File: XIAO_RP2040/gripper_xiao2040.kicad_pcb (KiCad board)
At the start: 2 copper layers, 11 parts, among them J1 GoFa IO, J2 VGoFa, J3 Servo, U1 XIAO-RP2040-DIP, U2 HCPL-2631

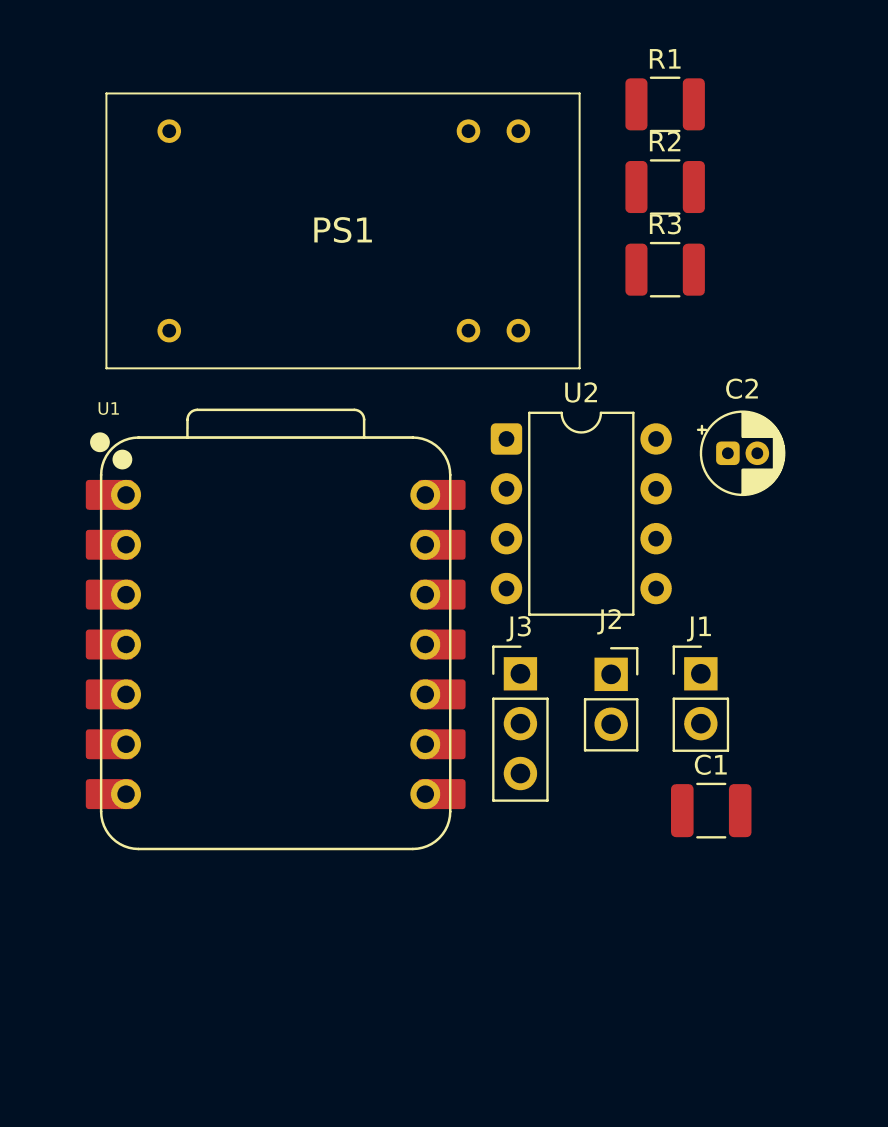
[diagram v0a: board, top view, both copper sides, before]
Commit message: Improving PCB routing and including Arduino code
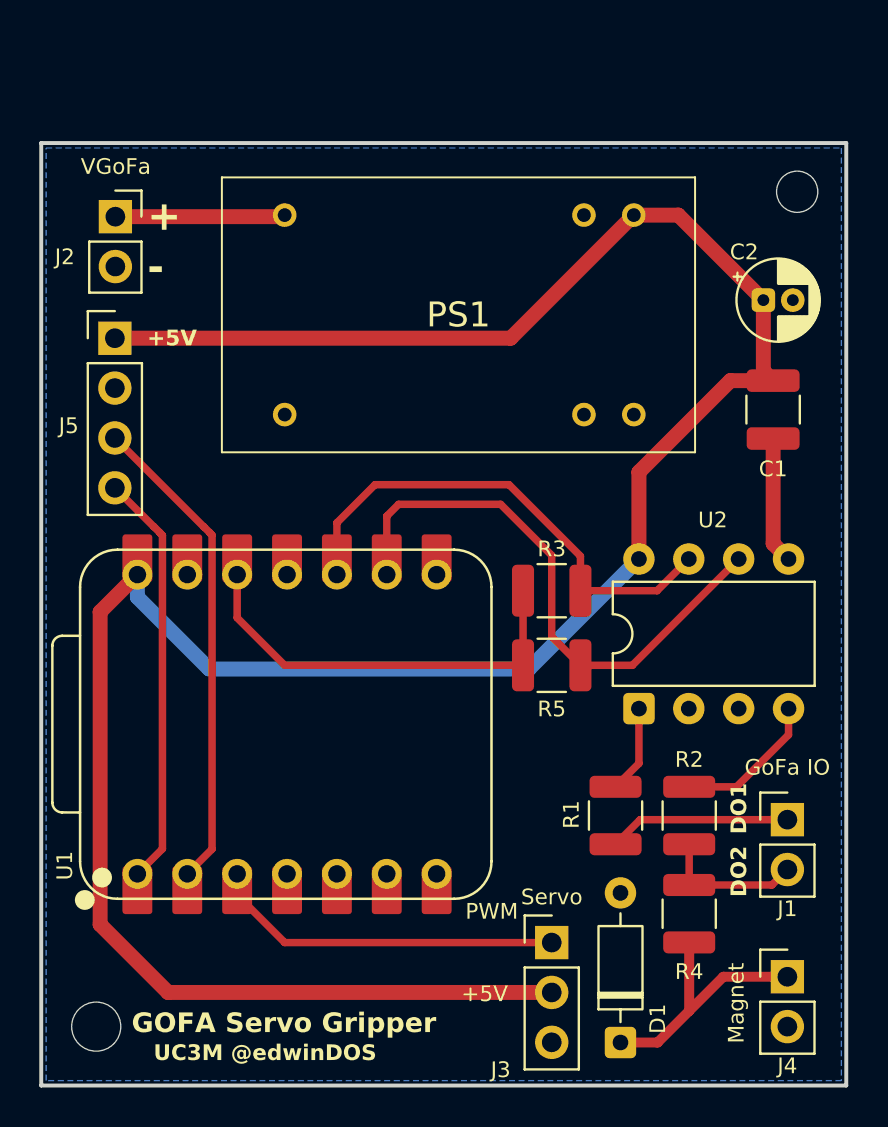
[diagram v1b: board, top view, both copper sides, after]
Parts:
- added D1: 1N4148, Diode_THT:D_DO-35_SOD27_P7.62mm_Horizontal, F.Cu at (150.5, 122.8)
- added J4: Magnet, Connector_PinHeader_2.54mm:PinHeader_1x02_P2.54mm_Vertical, F.Cu at (159.0, 119.5)
- added J5: Conn_01x04, Connector_PinHeader_2.54mm:PinHeader_1x04_P2.54mm_Vertical, F.Cu at (124.8, 86.9)
- added R4: R, Resistor_SMD:R_1210_3225Metric, F.Cu at (154.0, 116.2)
- added R5: R, Resistor_SMD:R_1210_3225Metric, F.Cu at (147.0, 103.6)
- added REF**: MountingHole_2.5mm, MountingHole:MountingHole_2.5mm, F.Cu at (123.8, 122.0)
- added REF**: MountingHole_2.1mm, MountingHole:MountingHole_2.1mm, F.Cu at (159.5, 79.5)
- C1: value C -> 100n
- C2: value C_Polarized -> 10uF
- moved R1 36.3 mm to (150.2, 111.2), turned to 90 degrees
- moved J2 34.4 mm to (124.8, 80.8)
- moved R2 32.0 mm to (154.0, 111.2), turned to -90 degrees
- moved C1 20.7 mm to (158.3, 90.6), turned to -90 degrees
- moved R3 17.3 mm to (147.0, 99.8)
- moved U2 15.3 mm to (151.4, 105.8), turned to 90 degrees
- moved J3 13.8 mm to (147.0, 117.7)
- moved J1 8.64 mm to (159.0, 111.5)
- moved C2 8.01 mm to (157.8, 85.0)
- moved PS1 7.27 mm to (133.4, 90.8)
- moved U1 4.10 mm to (133.5, 106.6), turned to 90 degrees
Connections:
- net Net-(J1-Pin_1) renamed /DO1
- net Net-(J1-Pin_2) renamed /DO2
- C1 pad 1: /Vcc -> +5V
- C2 pad 1: /Vcc -> +5V
- R3 pad 2: Net-(U1-GPIO29/ADC3/A3) -> /do1_coupled
- U1 pad 1: unconnected-(U1-GPIO26/ADC0/A0-Pad1) -> /A0
- U1 pad 10: unconnected-(U1-GPIO4/MISO-Pad10) -> /do1_coupled
- U1 pad 2: unconnected-(U1-GPIO27/ADC1/A1-Pad2) -> /D2
- U1 pad 4: Net-(U1-GPIO29/ADC3/A3) -> unconnected-(U1-GPIO29/ADC3/A3-Pad4)
- U1 pad 9: unconnected-(U1-GPIO2/SCK-Pad9) -> /do2_coupled
- U2 pad 6: unconnected-(U2-VO2-Pad6) -> /do2_coupled
- U2 pad 7: Net-(U1-GPIO29/ADC3/A3) -> /do1_coupled
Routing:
- net +5V: track 0.00 -> 128.5 mm
- net /do2_coupled: track 0.00 -> 29.2 mm
- net /D2: track 0.00 -> 25.9 mm
- net /do1_coupled: track 0.00 -> 24.5 mm
- net /A0: track 0.00 -> 22.3 mm
- net /+3V: track 0.00 -> 21.6 mm
- net /PWM: track 0.00 -> 18.1 mm
- net Net-(D1-K): track 0.00 -> 16.6 mm
- net /DO1: track 0.00 -> 9.27 mm
- net /Vcc: track 0.00 -> 8.66 mm
- net Net-(U2-A2): track 0.00 -> 7.49 mm
- net /DO2: track 0.00 -> 7.40 mm
- net GND: track 0.00 -> 6.46 mm
- net Net-(U2-A1): track 0.00 -> 4.48 mm
- added copper zone on B.Cu, net GND
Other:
- board outline added: 41 x 48 mm
- board text added: "+"
- board text added: "+5V"
- board text added: "-"
- board text added: "DO1"
- board text added: "DO2"
- board text added: "GOFA Servo Gripper"
- board text added: "PWM"
- board text added: "UC3M @edwinDOS"
